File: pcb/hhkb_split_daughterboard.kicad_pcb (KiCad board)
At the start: 2 copper layers, 21 x 32 mm, 11 parts

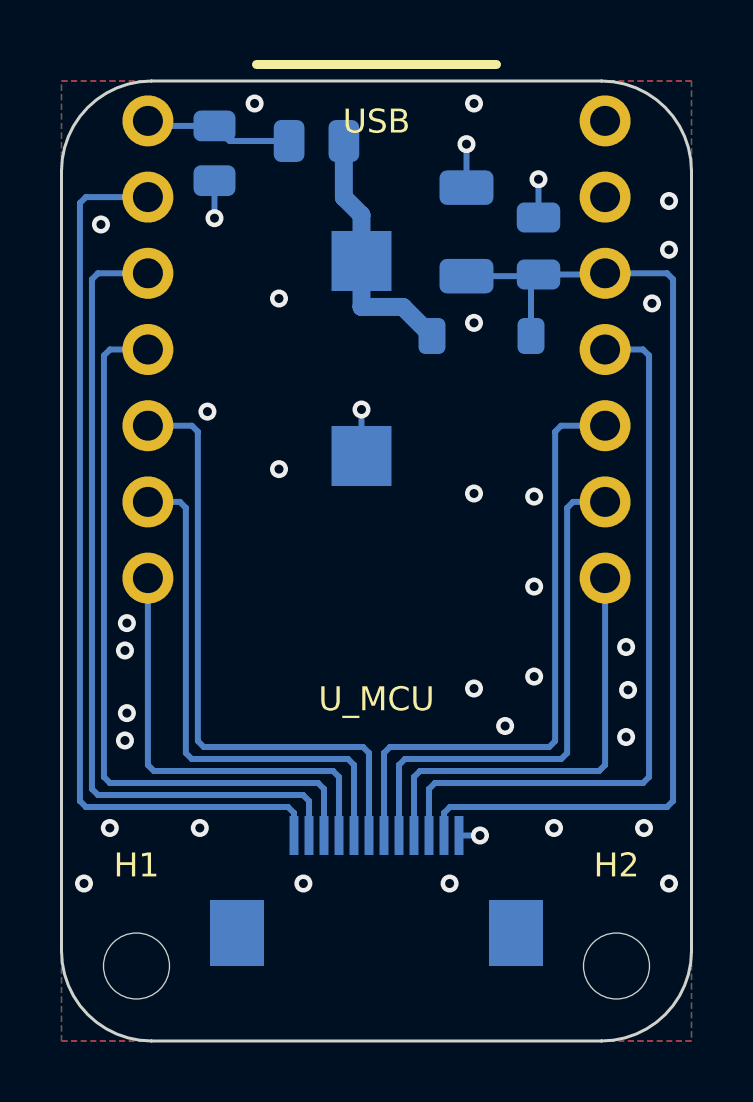
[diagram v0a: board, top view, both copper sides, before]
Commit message: 子基板のシルク位置を利用者の配置で確定させた（silk_overlap 5 → 0）
参照名のラベルが自分の部品の外形線に近すぎる警告が 5 件残っていた。
利用者が KiCad で 9 個を並べ直し、SILK_REF をその基板から
_read_silk_from で吸い出して更新した（手で書き写していない）。

子基板は 違反 0 / 未配線 0 / 警告 0。gen_daughterboard → autoroute で
再生成しても同じ配置が出ることを確認した。

⚠️ この更新には検査が付いていない。SW_PWR_1 を古い座標に戻して
再生成しても DRC は 0 件のままで、silk_overlap の再発を検出できない
（未配線基板では silk_overlap が常に 0 だった）。仕組みではなく
コメントの注意書きに頼っている。

なお .kicad_pro の solder_mask_to_copper_clearance が 0.005 に
なっていたのを 0.0 へ戻した（3 基板で揃った）。利用者は意図していない。

Co-Authored-By: Claude Opus 5 (1M context) <noreply@anthropic.com>
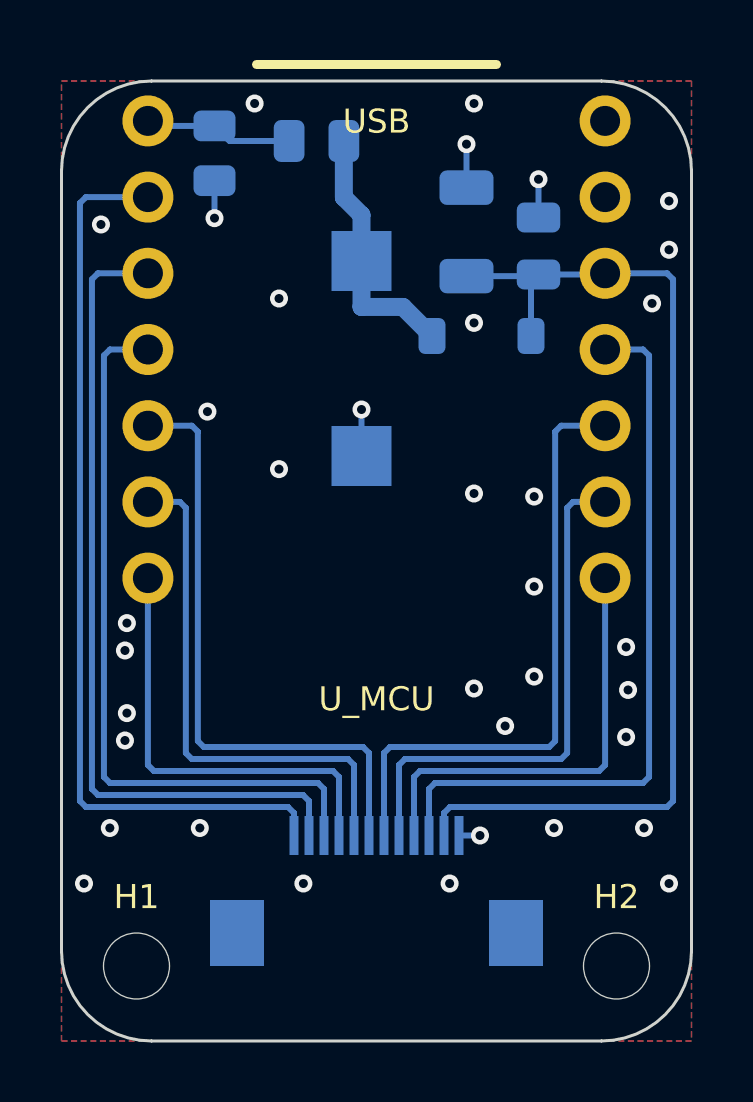
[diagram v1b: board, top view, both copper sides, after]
